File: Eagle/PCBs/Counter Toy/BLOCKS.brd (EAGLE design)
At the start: 16 parts, among them Q1 2N7002, Q5 2N7002, Q6 2N7002, Q9 2N7002, U2 TL072D

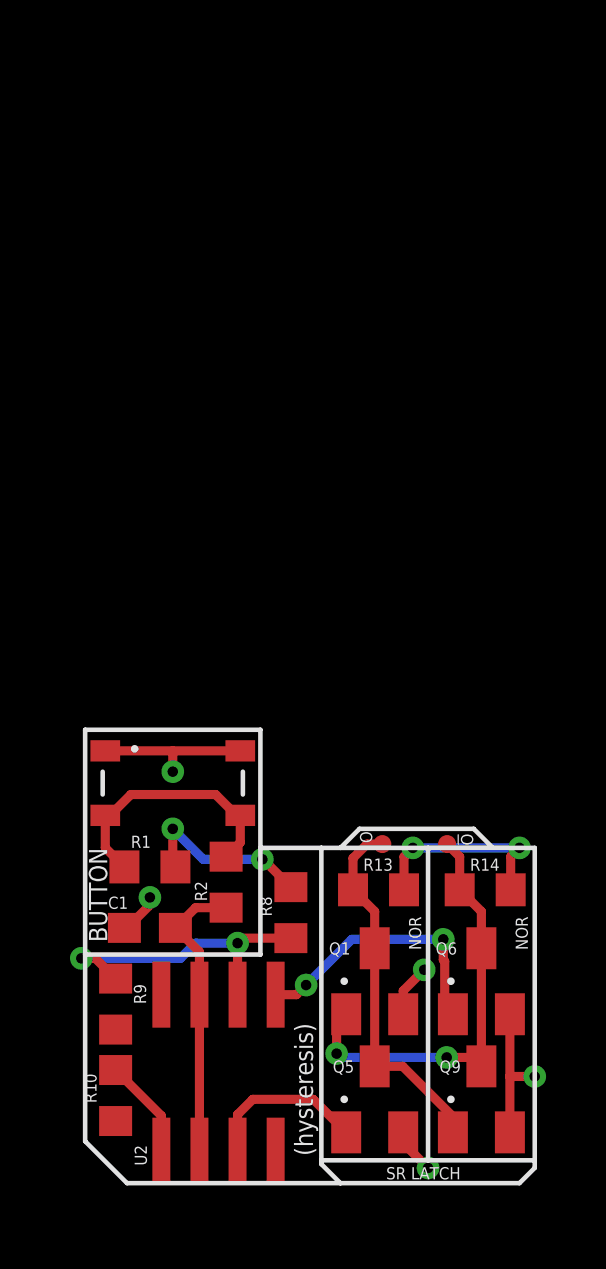
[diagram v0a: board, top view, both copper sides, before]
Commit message: Gave in and used a read schmitt trigger on my buttons
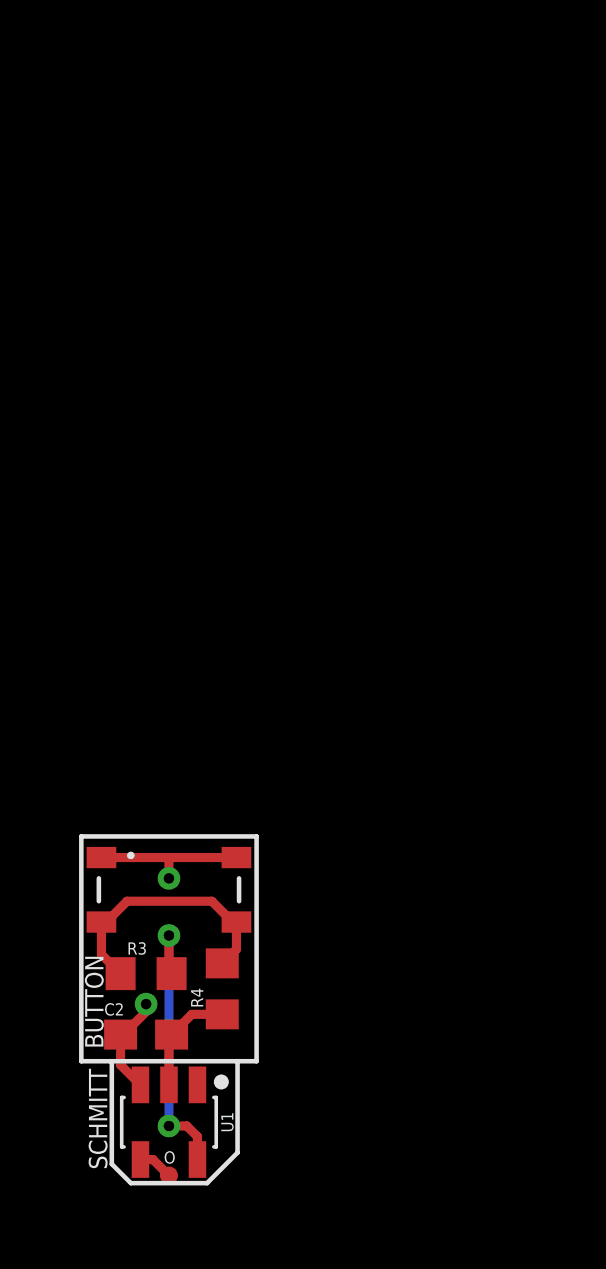
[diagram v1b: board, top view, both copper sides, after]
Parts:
- removed !O: TPPAD6, ellajameson-core:TP06R
- removed C1: 0.1u, ellajameson-core:C0603
- removed Q1, Q5, Q6, Q9: 2N7002, ellajameson-core:SOT23
- removed R1, R10, R2, R8, R9: 10k, ellajameson-core:R0603
- removed R13, R14: (no value), ellajameson-core:R0603
- removed S1: (no value), ellajameson-core:SW4_PTS815_SJM_250_SMTR_LFS_CN
- removed U2: TL072D, ellajameson-core:SO08
- added C2: 0.1u, ellajameson-core:C0603
- added R3, R4: 10k, ellajameson-core:R0603
- added S2: (no value), ellajameson-core:SW4_PTS815_SJM_250_SMTR_LFS_CN
- added U1: MC74HC1G14DTT1G, ellajameson-core:SOT95P275X110-5N
- moved O 13.1 mm to (2.79, 0.25), turned to 0 degrees
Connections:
- removed net N$13: Q5.1, U2.7
- removed net N$14: O.TP, Q1.3, Q5.3, Q9.1, R13.1
- removed net N$15: Q6.1, U2.1
- removed net N$16: !O.TP, Q1.1, Q6.3, Q9.3, R14.1
- removed net N$6: R10.2, R9.1, U2.5
- removed net N$7: R8.1, R9.2, U2.2
- removed net N$8: C1.1, R2.1, U2.3, U2.6
- new net N$1: O.TP, U1.4
- new net N$3: R3.1, R4.2, S2.3, S2.4
- net GND: now also C2.2, S2.1, S2.2, U1.3; no longer C1.2, Q1.2, Q5.2, Q6.2, Q9.2, R10.1, S1.1, S1.2, U2.4
- net N$4: now also C2.1, R4.1, U1.2; no longer R1.1, R2.2, S1.3, S1.4
- net VCC: now also R3.2, U1.5; no longer R1.2, R13.2, R14.2, R8.2, U2.8
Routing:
- net N$16: track 14.5 -> 0.00 mm, vias 2 -> 0
- net N$14: track 12.2 -> 0.00 mm
- net N$7: track 10.4 -> 0.00 mm, vias 2 -> 0
- net N$8: track 9.73 -> 0.00 mm
- net N$15: track 8.98 -> 0.00 mm, vias 2 -> 0
- net N$3: track 0.00 -> 8.63 mm
- net GND: track 14.7 -> 8.56 mm, vias 5 -> 2
- net N$13: track 5.49 -> 0.00 mm
- net N$4: track 8.63 -> 3.68 mm
- net N$6: track 3.32 -> 0.00 mm
- net VCC: track 12.6 -> 9.52 mm, vias 4 -> 2
- net N$1: track 0.00 -> 1.17 mm
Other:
- board text added: "SCHMITT"
- board text removed: "(hysteresis)"
- board text removed: "NOR"
- board text removed: "SR LATCH"

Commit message: Better DFF
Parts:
- removed C2: 0.1u, ellajameson-core:C0603
- removed O: TPPAD6, ellajameson-core:TP06R
- removed S2: (no value), ellajameson-core:SW4_PTS815_SJM_250_SMTR_LFS_CN
- removed U1: MC74HC1G14DTT1G, ellajameson-core:SOT95P275X110-5N
- added !Q, !R, CLK, D, Q: TPPAD6, ellajameson-core:TP06R
- added Q10, Q11, Q12, Q15, Q16, Q17, Q2, Q21, Q22, Q23, Q4, Q5, Q6, Q7, Q8, Q9: 2N7002, ellajameson-core:SOT23
- added R1, R5, R6, R8: (no value), ellajameson-core:R0603
- R3, R4: value 10k -> (none)
- moved R3 29.7 mm to (7.24, 36.2)
- moved R4 6.41 mm to (3.68, 12.8), turned to 0 degrees
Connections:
- removed net N$1: O.TP, U1.4
- removed net N$3: R3.1, R4.2, S2.3, S2.4
- new net N$10: Q2.2, Q5.3
- new net N$12: Q5.2, Q6.3
- new net N$14: Q4.2, Q7.3
- new net N$16: Q21.1, Q8.3, R5.1
- new net N$18: Q17.1, Q8.1, Q9.3, R4.1
- new net N$19: D.TP, Q10.1
- new net N$20: Q10.3, Q9.2
- new net N$22: Q10.2, Q11.3
- new net N$24: Q12.3, Q8.2
- new net N$31: CLK.TP, Q16.1, Q22.1
- new net N$32: Q15.2, Q16.3
- new net N$34: Q16.2, Q17.3
- new net N$44: Q21.2, Q22.3
- new net N$45: !R.TP, Q11.1, Q23.1, Q6.1
- new net N$46: Q22.2, Q23.3
- new net N$7: Q12.1, Q15.1, Q21.3, Q4.1, R8.1
- new net N$8: Q.TP, Q2.1, Q4.3, R3.1
- new net N$9: Q15.3, Q5.1, Q9.1, R6.1
- net GND: now also Q11.2, Q12.2, Q17.2, Q23.2, Q6.2, Q7.2; no longer C2.2, S2.1, S2.2, U1.3
- net N$4: now also !Q.TP, Q2.3, Q7.1, R1.1; no longer C2.1, R4.1, U1.2
- net VCC: now also R1.2, R4.2, R5.2, R6.2, R8.2; no longer U1.5
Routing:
- net VCC: track 9.52 -> 54.5 mm, vias 2 -> 6
- net N$8: track 0.00 -> 34.1 mm
- net N$7: track 0.00 -> 30.8 mm, vias 0 -> 2
- net N$9: track 0.00 -> 29.3 mm, vias 0 -> 2
- net N$18: track 0.00 -> 25.0 mm
- net N$4: track 3.68 -> 28.6 mm, vias 0 -> 3
- net N$45: track 0.00 -> 20.0 mm, vias 0 -> 2
- net N$16: track 0.00 -> 14.2 mm, vias 0 -> 2
- net N$31: track 0.00 -> 12.2 mm, vias 0 -> 3
- net GND: track 8.56 -> 18.5 mm, vias 2 -> 5
- net N$3: track 8.63 -> 0.00 mm
- net N$32: track 0.00 -> 2.75 mm
- net N$24: track 0.00 -> 2.75 mm
- net N$44: track 0.00 -> 2.75 mm
- net N$20: track 0.00 -> 2.75 mm
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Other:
- board text added: "DFF"
- board text added: "NAND"
- board text added: "NAND3"
- board text removed: "BUTTON"
- board text removed: "SCHMITT"
